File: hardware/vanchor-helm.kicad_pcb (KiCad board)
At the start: 2 copper layers, 160 x 120 mm, 112 parts, among them J1 PI_40PIN_STACK, J10 DISP PWR 5V, J11 AS5600, J12 PICO UTIL, J17 12V_LINK, J18 LUG BATT+, J19 LUG MOTOR A, J2 PI_BREAKOUT, J20 LUG MOTOR B, J21 LUG GND, J22 SERVO MOTOR, J3 UART0 ttyAMA0, J4 UART2 ttyAMA2, J5 UART3 ttyAMA3, J6 UART4 ttyAMA4, J7 UART5 ttyAMA5, J8 I2C1 spare, J9 FAN 5V, Q1 IRF9540N, Q10 IRF100P219, Q3 IRF100P219, Q4 IRF100P219, Q5 IRF100P219, Q6 IRF100P219, Q7 IRF100P219, Q8 IRF100P219, Q9 IRF100P219, U1 Pico 2, U10 ACS758LCB-100B, U5 D36V50F5, U6 D36V50F12, U7 BTN8982TA, U8 BTN8982TA, U9 HIP4082IPZ

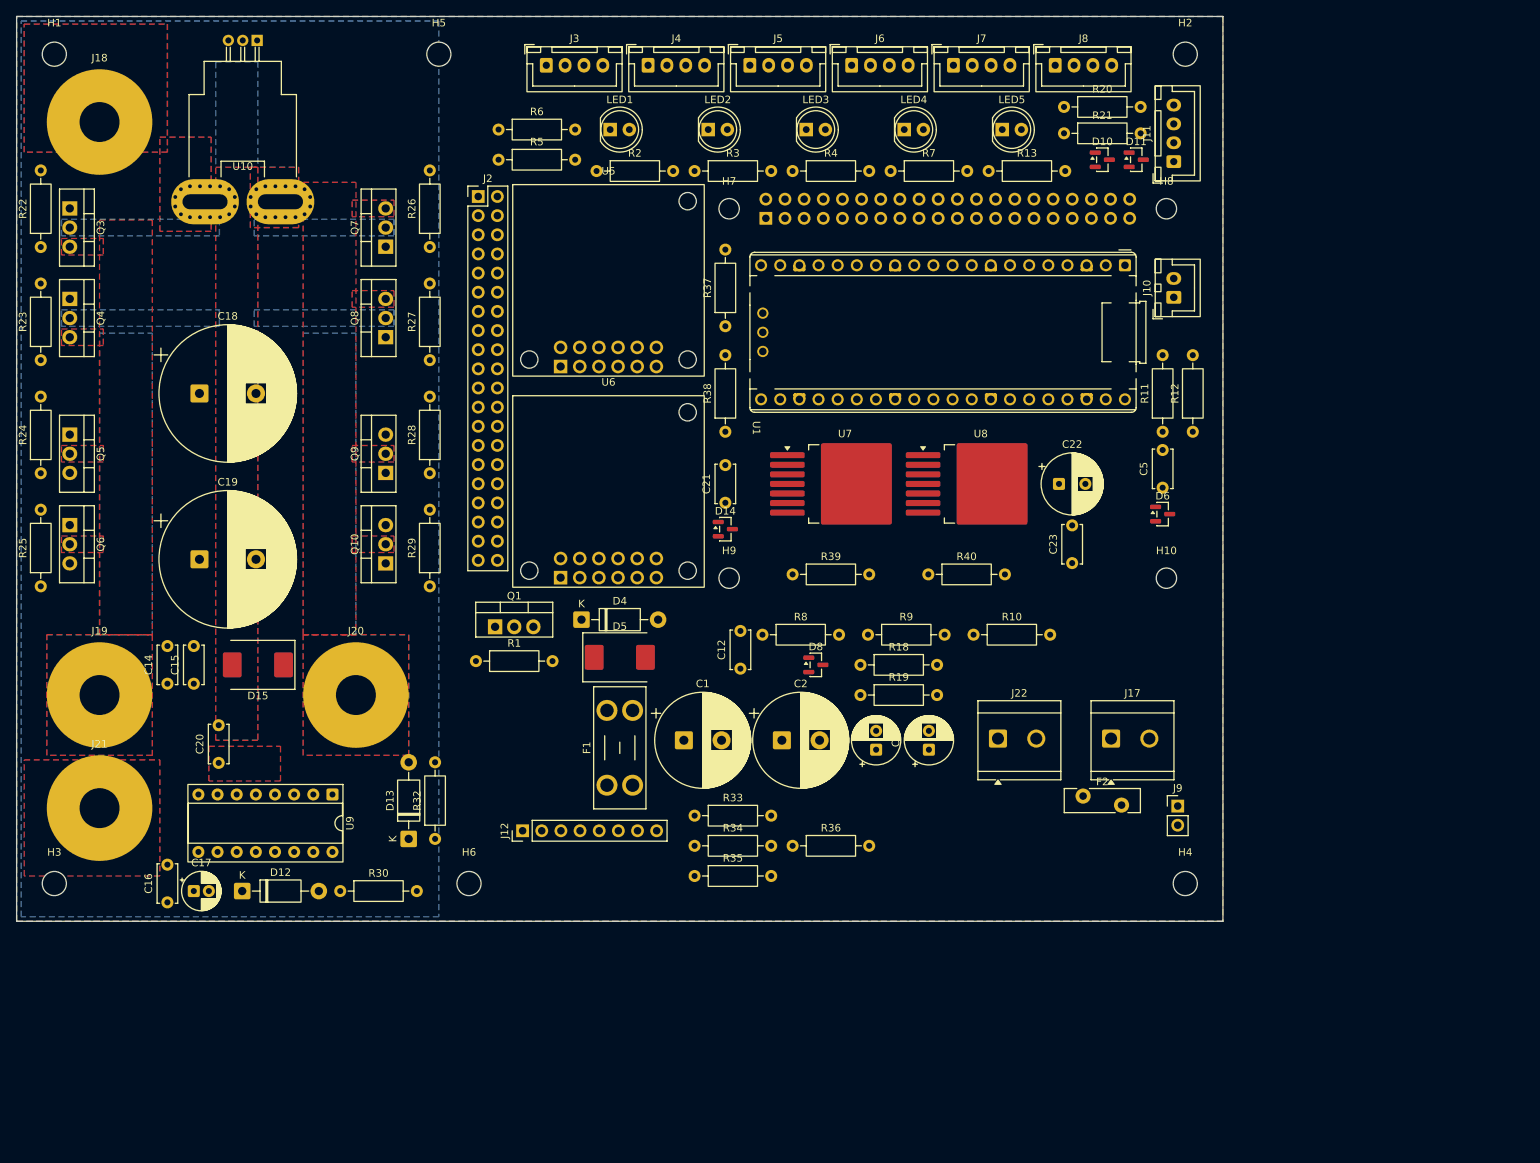
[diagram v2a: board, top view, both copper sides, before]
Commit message: feat: pre-laid power spine tracks + BASE_GND flag + GND stitching in import
Co-Authored-By: Claude Fable 5 <noreply@anthropic.com>
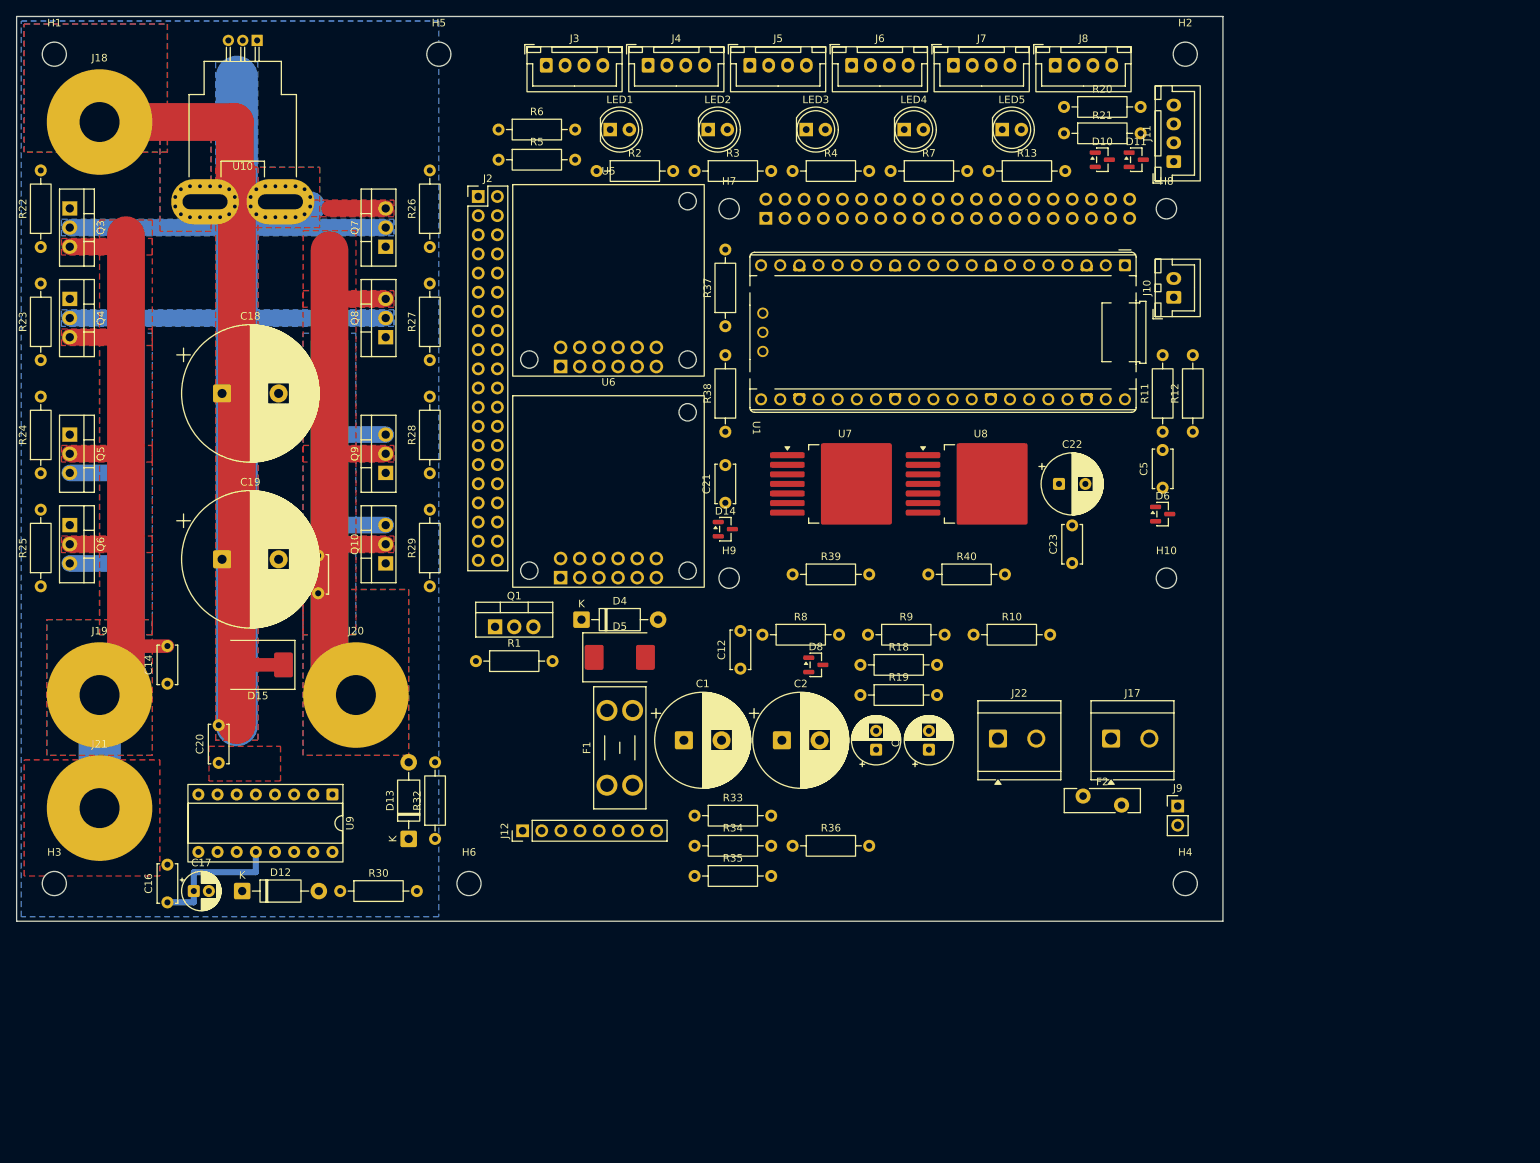
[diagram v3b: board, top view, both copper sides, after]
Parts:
- moved C15 20.4 mm to (60.0, 96.5)
- moved C18 3.00 mm to (47.2, 70.0)
- moved C19 3.00 mm to (47.2, 92.0)
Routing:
- net VBRIDGE: track 0.00 -> 263.1 mm
- net MOTOR_A: track 0.00 -> 150.3 mm
- net MOTOR_B: track 0.00 -> 144.3 mm
- net VBAT_PWR: track 0.00 -> 58.3 mm
- net GND: track 0.00 -> 35.0 mm
- net +12V: track 0.00 -> 18.4 mm

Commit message: feat: routed board via scripted freerouting pipeline (T10) — known GUI touch-up items documented
Co-Authored-By: Claude Fable 5 <noreply@anthropic.com>
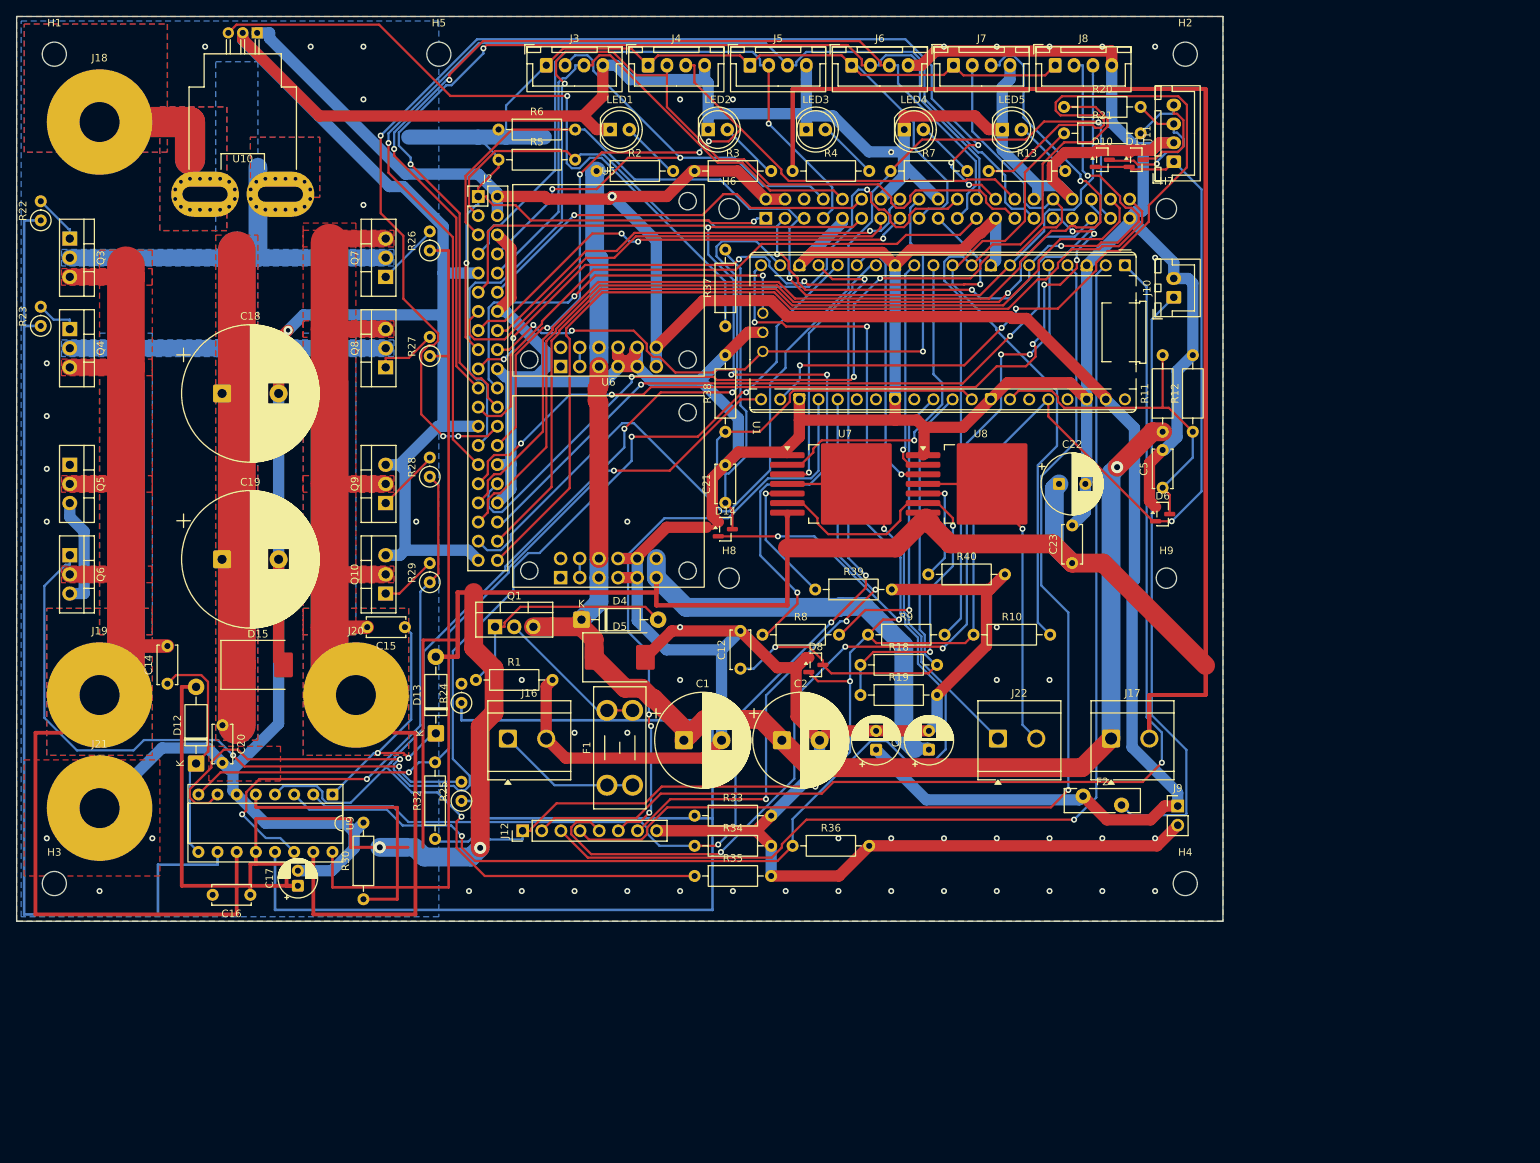
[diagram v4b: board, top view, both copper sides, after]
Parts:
- removed H10: MountingHole_2.7mm_M2.5, MountingHole_2.7mm_M2.5
- added J16: LOGIC 12-48V, TerminalBlock_CUI_TB007-508-02_1x02_P5.08mm_Horizontal, F.Cu at (85.2, 115.8)
- H6: value MountingHole_3.2mm_M3 -> MountingHole_2.7mm_M2.5; footprint MountingHole_3.2mm_M3 -> MountingHole_2.7mm_M2.5
- R22, R23, R24, R25, R26, R27, R28, R29: footprint R_Axial_DIN0207_L6.3mm_D2.5mm_P10.16mm_Horizontal -> R_Axial_DIN0207_L6.3mm_D2.5mm_P2.54mm_Vertical
- moved H6 95.9 mm to (114.5, 45.5)
- moved H8 75.9 mm to (114.5, 94.5)
- moved R24 63.6 mm to (79.0, 111.0)
- moved R25 62.6 mm to (79.0, 124.0)
- moved H7 58.0 mm to (172.5, 45.5)
- moved H9 58.0 mm to (172.5, 94.5)
- moved D12 18.0 mm to (43.8, 119.1), turned to 90 degrees
- moved D13 14.5 mm to (75.6, 115.1)
- moved C17 13.8 mm to (57.3, 135.3), turned to 90 degrees
- moved C15 12.3 mm to (71.5, 101.0), turned to 180 degrees
- moved C16 11.0 mm to (51.0, 136.5), turned to 180 degrees
- moved C20 5.02 mm to (47.3, 114.0), turned to -90 degrees
- moved R23 4.53 mm to (23.2, 61.0)
- moved Q8 4.00 mm to (69.0, 66.5)
- moved Q10 4.00 mm to (69.0, 96.5)
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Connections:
- F1 pad 1: VBAT_PWR -> /power/BATT_IN
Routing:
- net GND: track 35.0 -> 1149.0 mm, vias 0 -> 54
- net +12V: track 18.4 -> 697.6 mm, vias 0 -> 2
- net +5V: track 0.00 -> 281.4 mm, vias 0 -> 1
- net +3V3: track 0.00 -> 253.9 mm, vias 0 -> 5
- net 3V3_PI: track 0.00 -> 205.4 mm, vias 0 -> 2
- net VIN: track 0.00 -> 196.4 mm, vias 0 -> 1
- net THR_BLI: track 0.00 -> 184.9 mm, vias 0 -> 3
- net THR_ALI: track 0.00 -> 173.9 mm, vias 0 -> 3
- net /thrust/ALO: track 0.00 -> 162.1 mm
- net PI_GPIO7: track 0.00 -> 159.0 mm, vias 0 -> 6
- net UART3_RX: track 0.00 -> 155.7 mm, vias 0 -> 1
- net PICO_GP0: track 0.00 -> 154.0 mm, vias 0 -> 1
- net THR_BHI: track 0.00 -> 148.9 mm, vias 0 -> 4
- net THR_AHI: track 0.00 -> 147.2 mm, vias 0 -> 3
- net PICO_GP1: track 0.00 -> 147.1 mm, vias 0 -> 1
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
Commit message: feat: v2 board 200x150mm — DRC clean, zero touch-up (fresh layout, 2x spacing)
Co-Authored-By: Claude Fable 5 <noreply@anthropic.com>
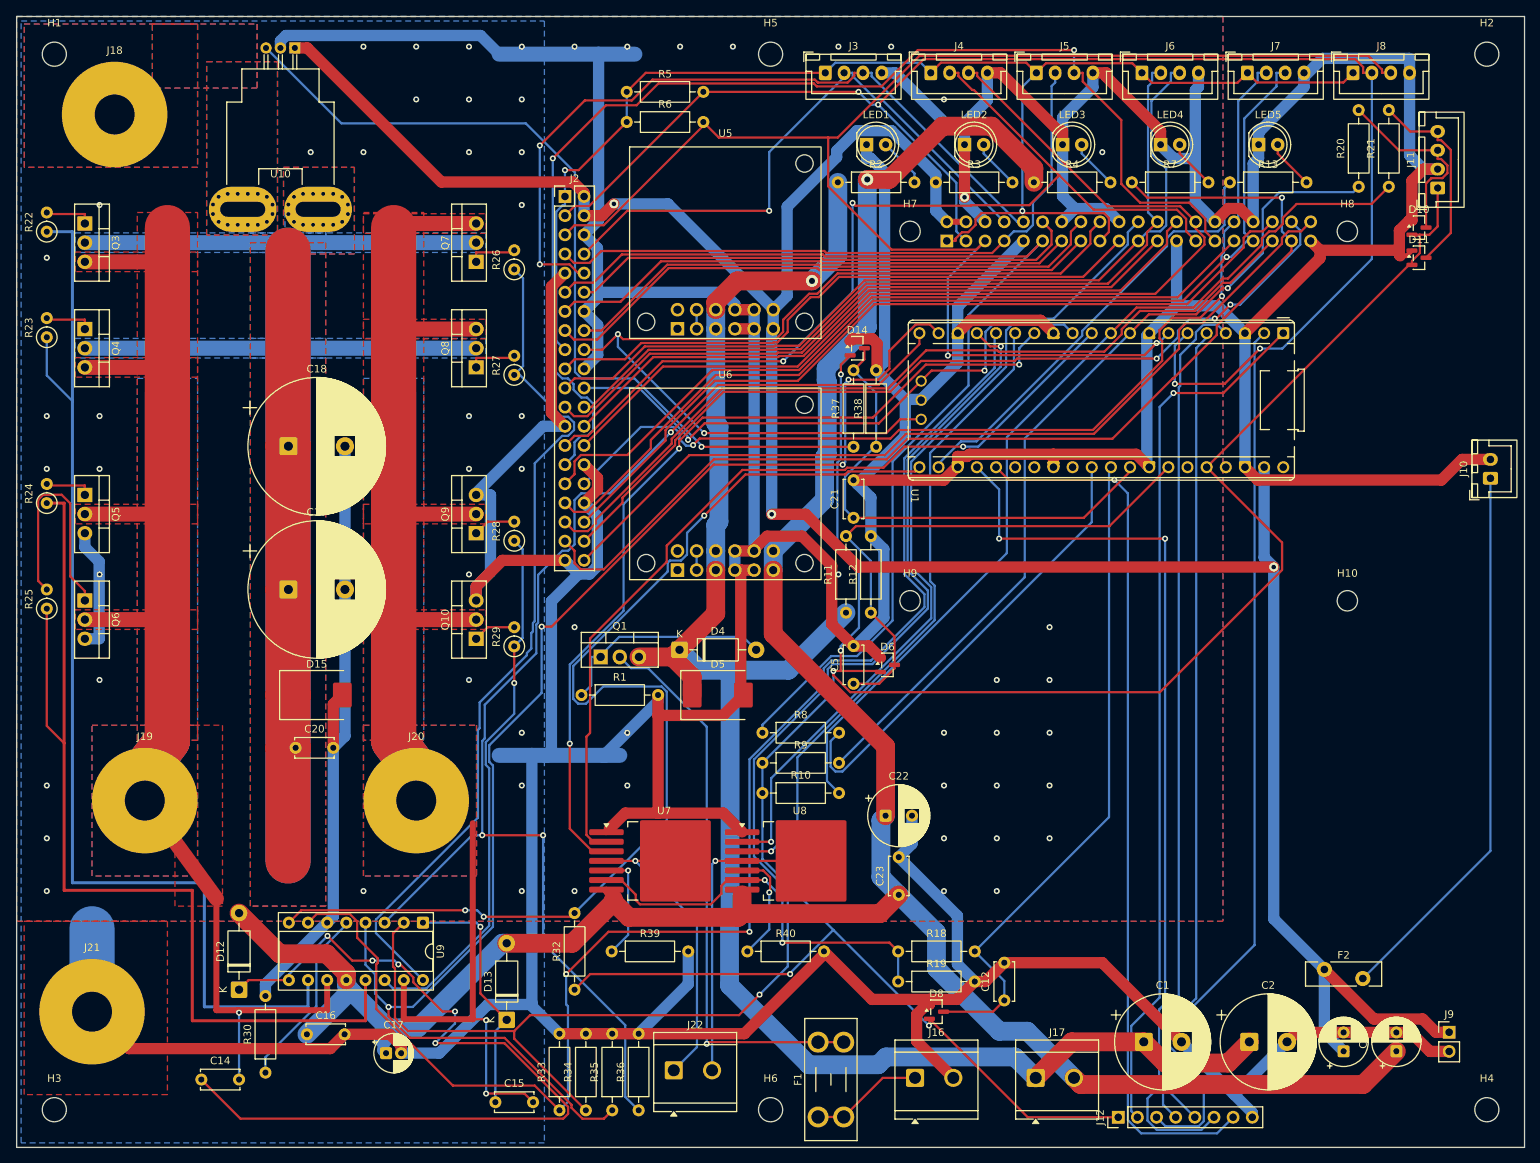
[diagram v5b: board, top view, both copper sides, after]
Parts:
- added H10: MountingHole_2.7mm_M2.5, MountingHole_2.7mm_M2.5, F.Cu at (196.5, 97.5)
- H6: value MountingHole_2.7mm_M2.5 -> MountingHole_3.2mm_M3; footprint MountingHole_2.7mm_M2.5 -> MountingHole_3.2mm_M3
- moved H6 119.6 mm to (120.0, 165.0)
- moved H8 94.0 mm to (196.5, 48.5)
- moved J12 87.7 mm to (166.1, 166.0)
- moved C2 73.8 mm to (183.5, 156.0)
- moved C3 73.8 mm to (196.0, 157.2)
- moved C4 73.8 mm to (203.0, 157.2)
- moved C1 72.9 mm to (169.5, 156.0)
- moved J16 70.3 mm to (139.2, 160.8)
- moved C15 64.1 mm to (83.5, 164.0), turned to 0 degrees
- moved J22 61.5 mm to (107.2, 159.8)
- moved R24 61.1 mm to (24.0, 84.5)
- moved R25 60.6 mm to (24.0, 98.5)
- moved C12 56.2 mm to (151.0, 150.5)
- moved R40 55.5 mm to (116.9, 144.0)
- moved U7 55.5 mm to (105.9, 132.0)
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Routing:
- net +12V: track 697.6 -> 338.8 mm, vias 2 -> 1
- net GND: track 1149.0 -> 1302.9 mm, vias 54 -> 61
- net /thrust/AHB: track 30.3 -> 115.0 mm, vias 0 -> 5
- net R_EN: track 34.5 -> 117.8 mm, vias 1 -> 3
- net RPWM: track 43.7 -> 113.8 mm
- net PI_GPIO7: track 159.0 -> 90.8 mm, vias 6 -> 0
- net PI_SCL: track 134.1 -> 201.5 mm, vias 1 -> 2
- net LPWM: track 29.2 -> 96.4 mm
- net PI_SDA: track 140.8 -> 206.2 mm
- net LED_STAT: track 123.3 -> 58.4 mm, vias 3 -> 0
- net +3V3: track 253.9 -> 317.4 mm
- net /power/VIN_RAW: track 20.3 -> 75.7 mm, vias 0 -> 1
- net /thrust/G_AL2: track 83.5 -> 31.1 mm, vias 2 -> 0
- net L_EN: track 36.4 -> 86.5 mm
- net +5V: track 281.4 -> 330.1 mm, vias 1 -> 3
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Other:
- board size 160 x 120 mm -> 200 x 150 mm
